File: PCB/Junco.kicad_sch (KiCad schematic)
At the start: 202 parts, among them J1 AudioJack4, J2 AudioJack4, SW1 SW_Push, SW10 SW_Push, SW11 SW_Push, SW12 SW_Push, SW13 SW_Push, SW14 SW_Push, SW15 SW_Push, SW16 SW_Push, SW17 SW_Push, SW18 SW_Push, SW19 SW_MX_Hotswap_Rotary, SW2 SW_Push, SW20 SW_Push, SW21 SW_Push, SW22 SW_Push, SW23 SW_Push, SW24 SW_Push, SW25 SW_Push, SW26 SW_Push, SW27 SW_Push, SW28 SW_Push, SW29 SW_Push, SW3 SW_Push, SW30 RotaryEncoder_Switch, SW31 SW_Push, SW32 SW_Push, SW33 SW_Push, SW34 SW_Push, SW35 SW_Push, SW36 SW_Push, SW37 SW_Push, SW38 SW_Push, SW39 SW_Push, SW4 SW_Push, SW40 SW_Push, SW41 SW_Push, SW42 SW_Push, SW43 SW_Push, SW44 SW_Push, SW45 SW_Push, SW46 SW_Push, SW47 SW_Push, SW48 SW_Push, SW49 SW_MX_Hotswap_Rotary, SW5 SW_Push, SW50 SW_Push, SW51 SW_Push, SW52 SW_Push, SW53 SW_Push, SW54 SW_Push, SW55 SW_Push, SW56 SW_Push, SW57 SW_Push, SW58 SW_Push, SW59 SW_Push, SW6 SW_Push, SW60 RotaryEncoder_Switch, SW7 SW_Push, SW8 SW_Push, SW9 SW_Push, U1 Pico, U2 SN74AHCT1G125, U3 Pico, U4 SN74AHCT1G125

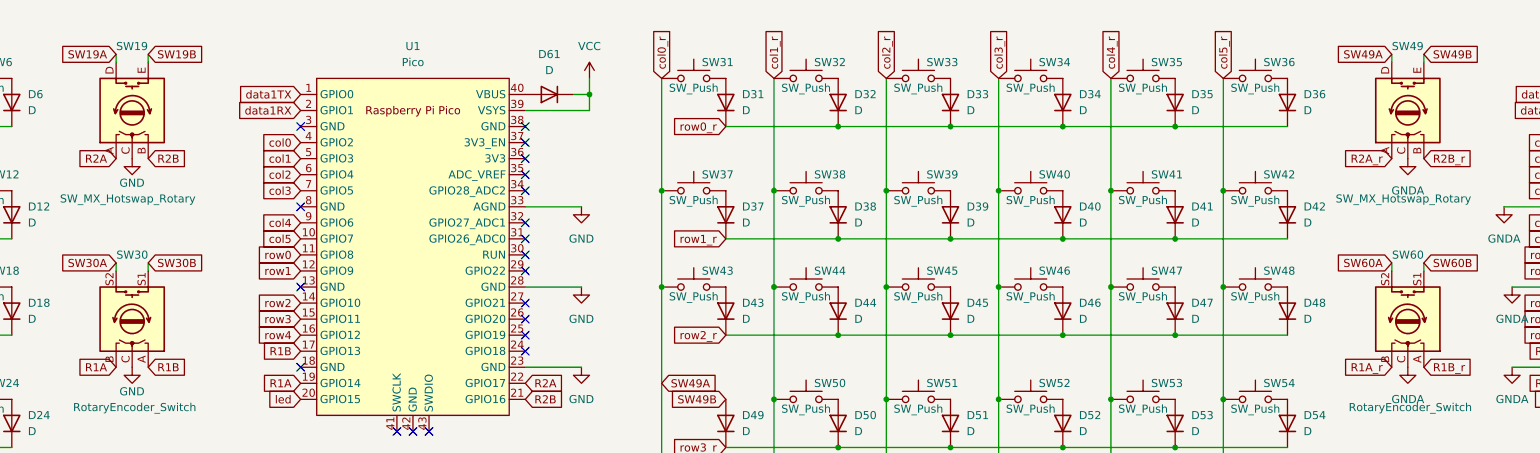
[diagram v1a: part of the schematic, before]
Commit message: Keycap rotation Swapped in smd/through-hole diode footprints
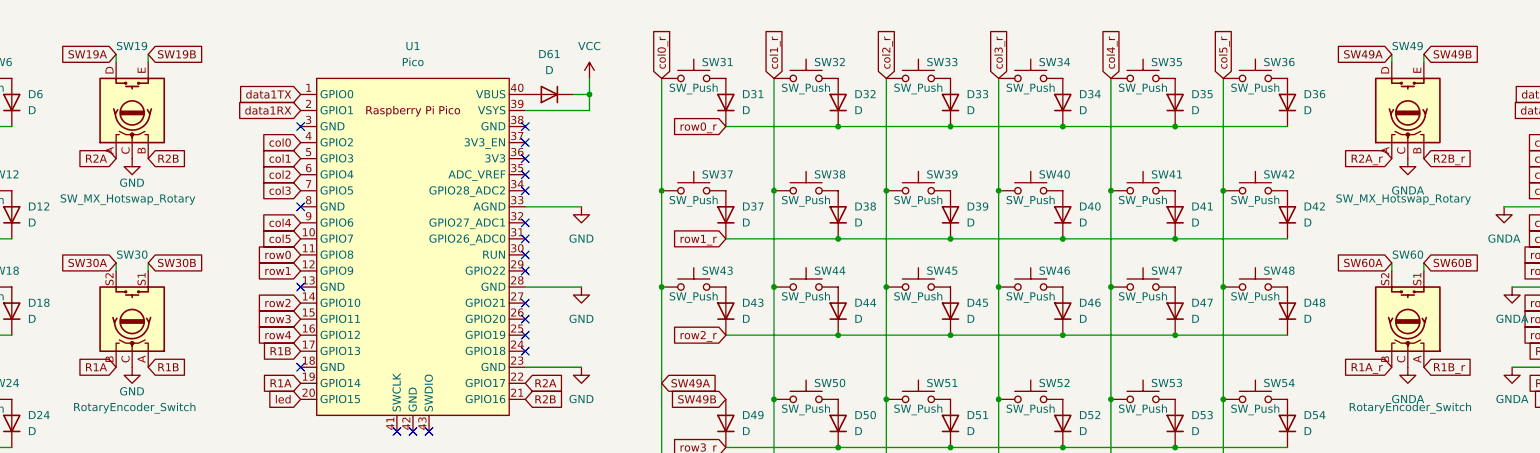
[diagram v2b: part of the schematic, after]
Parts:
- D1, D10, D11, D12, D13, D14, D15, D16, D17, D18, D19, D2, D20, D21, D22, D23, D24, D25, D26, D27, D28, D29, D3, D30, D31, D32, D33, D34, D35, D36, D37, D38, D39, D4, D40, D41, D42, D43, D44, D45, D46, D47, D48, D49, D5, D50, D51, D52, D53, D54, D55, D56, D57, D58, D59, D6, D60, D61, D62, D7, D8, D9: footprint Junco:D_SOD-123 -> Junco:D_SOD-123_DO-35_Hybrid_DoubleSided_V2

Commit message: comitt before pcb led rotation unification already updated LED orientation on schematic
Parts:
- SK68XX_Mini10, SK68XX_Mini11, SK68XX_Mini12, SK68XX_Mini13, SK68XX_Mini14, SK68XX_Mini21, SK68XX_Mini22, SK68XX_Mini23, SK68XX_Mini24, SK68XX_Mini25, SK68XX_Mini26, SK68XX_Mini35, SK68XX_Mini36, SK68XX_Mini37, SK68XX_Mini52, SK68XX_Mini53, SK68XX_Mini54, SK68XX_Mini55, SK68XX_Mini56, SK68XX_Mini57, SK68XX_Mini64, SK68XX_Mini65, SK68XX_Mini66, SK68XX_Mini67, SK68XX_Mini68, SK68XX_Mini69, SK68XX_Mini70, SK68XX_Mini71, SK68XX_Mini9: footprint Junco:SK68XXMini_Offset_Flipped -> Junco:SK68XXMini_Offset
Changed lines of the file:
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@@
       (effects (font (size 1.27 1.27)) hide)
     )
-    (property "Footprint" "Junco:SK68XXMini_Offset_Flipped" (at 387.35 165.1 0)
+    (property "Footprint" "Junco:SK68XXMini_Offset" (at 387.35 165.1 0)
       (effects (font (size 1.27 1.27)) hide)
     )
@@
       (effects (font (size 1.27 1.27)) hide)
     )
-    (property "Footprint" "Junco:SK68XXMini_Offset_Flipped" (at 52.07 175.26 0)
+    (property "Footprint" "Junco:SK68XXMini_Offset" (at 52.07 175.26 0)
       (effects (font (size 1.27 1.27)) hide)
     )
@@
       (effects (font (size 1.27 1.27)) hide)
     )
-    (property "Footprint" "Junco:SK68XXMini_Offset_Flipped" (at 359.41 205.74 0)
+    (property "Footprint" "Junco:SK68XXMini_Offset" (at 359.41 205.74 0)
       (effects (font (size 1.27 1.27)) hide)
     )
@@
       (effects (font (size 1.27 1.27)) hide)
     )
-    (property "Footprint" "Junco:SK68XXMini_Offset_Flipped" (at 31.75 236.22 0)
+    (property "Footprint" "Junco:SK68XXMini_Offset" (at 31.75 236.22 0)
       (effects (font (size 1.27 1.27)) hide)
     )
@@
       (effects (font (size 1.27 1.27)) hide)
     )
-    (property "Footprint" "Junco:SK68XXMini_Offset_Flipped" (at 59.69 154.94 0)
+    (property "Footprint" "Junco:SK68XXMini_Offset" (at 59.69 154.94 0)
       (effects (font (size 1.27 1.27)) hide)
     )
@@
       (effects (font (size 1.27 1.27)) hide)
     )
-    (property "Footprint" "Junco:SK68XXMini_Offset_Flipped" (at 339.09 226.06 0)
+    (property "Footprint" "Junco:SK68XXMini_Offset" (at 339.09 226.06 0)
       (effects (font (size 1.27 1.27)) hide)
     )
@@
       (effects (font (size 1.27 1.27)) hide)
     )
-    (property "Footprint" "Junco:SK68XXMini_Offset_Flipped" (at 31.75 154.94 0)
+    (property "Footprint" "Junco:SK68XXMini_Offset" (at 31.75 154.94 0)
       (effects (font (size 1.27 1.27)) hide)
     )
@@
       (effects (font (size 1.27 1.27)) hide)
     )
-    (property "Footprint" "Junco:SK68XXMini_Offset_Flipped" (at 24.13 215.9 0)
+    (property "Footprint" "Junco:SK68XXMini_Offset" (at 24.13 215.9 0)
       (effects (font (size 1.27 1.27)) hide)
     )
@@
       (effects (font (size 1.27 1.27)) hide)
     )
-    (property "Footprint" "Junco:SK68XXMini_Offset_Flipped" (at 367.03 226.06 0)
+    (property "Footprint" "Junco:SK68XXMini_Offset" (at 367.03 226.06 0)
       (effects (font (size 1.27 1.27)) hide)
     )
@@
       (effects (font (size 1.27 1.27)) hide)
     )
-    (property "Footprint" "Junco:SK68XXMini_Offset_Flipped" (at 115.57 195.58 0)
+    (property "Footprint" "Junco:SK68XXMini_Offset" (at 115.57 195.58 0)
       (effects (font (size 1.27 1.27)) hide)
     )
@@
       (effects (font (size 1.27 1.27)) hide)
     )
-    (property "Footprint" "Junco:SK68XXMini_Offset_Flipped" (at 87.63 195.58 0)
+    (property "Footprint" "Junco:SK68XXMini_Offset" (at 87.63 195.58 0)
       (effects (font (size 1.27 1.27)) hide)
     )
@@
       (effects (font (size 1.27 1.27)) hide)
     )
-    (property "Footprint" "Junco:SK68XXMini_Offset_Flipped" (at 115.57 154.94 0)
+    (property "Footprint" "Junco:SK68XXMini_Offset" (at 115.57 154.94 0)
       (effects (font (size 1.27 1.27)) hide)
     )
@@
       (effects (font (size 1.27 1.27)) hide)
     )
-    (property "Footprint" "Junco:SK68XXMini_Offset_Flipped" (at 359.41 165.1 0)
+    (property "Footprint" "Junco:SK68XXMini_Offset" (at 359.41 165.1 0)
       (effects (font (size 1.27 1.27)) hide)
     )
@@
       (effects (font (size 1.27 1.27)) hide)
     )
-    (property "Footprint" "Junco:SK68XXMini_Offset_Flipped" (at 59.69 195.58 0)
+    (property "Footprint" "Junco:SK68XXMini_Offset" (at 59.69 195.58 0)
       (effects (font (size 1.27 1.27)) hide)
     )
@@
       (effects (font (size 1.27 1.27)) hide)
     )
-    (property "Footprint" "Junco:SK68XXMini_Offset_Flipped" (at 303.53 165.1 0)
+    (property "Footprint" "Junco:SK68XXMini_Offset" (at 303.53 165.1 0)
       (effects (font (size 1.27 1.27)) hide)
     )
@@
       (effects (font (size 1.27 1.27)) hide)
     )
-    (property "Footprint" "Junco:SK68XXMini_Offset_Flipped" (at 311.15 226.06 0)
+    (property "Footprint" "Junco:SK68XXMini_Offset" (at 311.15 226.06 0)
       (effects (font (size 1.27 1.27)) hide)
     )
@@
       (effects (font (size 1.27 1.27)) hide)
     )
-    (property "Footprint" "Junco:SK68XXMini_Offset_Flipped" (at 303.53 205.74 0)
+    (property "Footprint" "Junco:SK68XXMini_Offset" (at 303.53 205.74 0)
       (effects (font (size 1.27 1.27)) hide)
     )
@@
       (effects (font (size 1.27 1.27)) hide)
     )
-    (property "Footprint" "Junco:SK68XXMini_Offset_Flipped" (at 394.97 185.42 0)
+    (property "Footprint" "Junco:SK68XXMini_Offset" (at 394.97 185.42 0)
       (effects (font (size 1.27 1.27)) hide)
     )
@@
       (effects (font (size 1.27 1.27)) hide)
     )
-    (property "Footprint" "Junco:SK68XXMini_Offset_Flipped" (at 387.35 205.74 0)
+    (property "Footprint" "Junco:SK68XXMini_Offset" (at 387.35 205.74 0)
       (effects (font (size 1.27 1.27)) hide)
     )
@@
       (effects (font (size 1.27 1.27)) hide)
     )
-    (property "Footprint" "Junco:SK68XXMini_Offset_Flipped" (at 394.97 226.06 0)
+    (property "Footprint" "Junco:SK68XXMini_Offset" (at 394.97 226.06 0)
       (effects (font (size 1.27 1.27)) hide)
     )
@@
       (effects (font (size 1.27 1.27)) hide)
     )
-    (property "Footprint" "Junco:SK68XXMini_Offset_Flipped" (at 331.47 205.74 0)
+    (property "Footprint" "Junco:SK68XXMini_Offset" (at 331.47 205.74 0)
       (effects (font (size 1.27 1.27)) hide)
     )
@@
       (effects (font (size 1.27 1.27)) hide)
     )
-    (property "Footprint" "Junco:SK68XXMini_Offset_Flipped" (at 331.47 165.1 0)
+    (property "Footprint" "Junco:SK68XXMini_Offset" (at 331.47 165.1 0)
       (effects (font (size 1.27 1.27)) hide)
     )
@@
       (effects (font (size 1.27 1.27)) hide)
     )
-    (property "Footprint" "Junco:SK68XXMini_Offset_Flipped" (at 24.13 175.26 0)
+    (property "Footprint" "Junco:SK68XXMini_Offset" (at 24.13 175.26 0)
       (effects (font (size 1.27 1.27)) hide)
     )
@@
       (effects (font (size 1.27 1.27)) hide)
     )
-    (property "Footprint" "Junco:SK68XXMini_Offset_Flipped" (at 31.75 195.58 0)
+    (property "Footprint" "Junco:SK68XXMini_Offset" (at 31.75 195.58 0)
       (effects (font (size 1.27 1.27)) hide)
     )
@@
       (effects (font (size 1.27 1.27)) hide)
     )
-    (property "Footprint" "Junco:SK68XXMini_Offset_Flipped" (at 59.69 236.22 0)
+    (property "Footprint" "Junco:SK68XXMini_Offset" (at 59.69 236.22 0)
       (effects (font (size 1.27 1.27)) hide)
     )
@@
       (effects (font (size 1.27 1.27)) hide)
     )
-    (property "Footprint" "Junco:SK68XXMini_Offset_Flipped" (at 87.63 154.94 0)
+    (property "Footprint" "Junco:SK68XXMini_Offset" (at 87.63 154.94 0)
       (effects (font (size 1.27 1.27)) hide)
     )
@@
       (effects (font (size 1.27 1.27)) hide)
     )
-    (property "Footprint" "Junco:SK68XXMini_Offset_Flipped" (at 367.03 185.42 0)
+    (property "Footprint" "Junco:SK68XXMini_Offset" (at 367.03 185.42 0)
       (effects (font (size 1.27 1.27)) hide)
     )
@@
       (effects (font (size 1.27 1.27)) hide)
     )
-    (property "Footprint" "Junco:SK68XXMini_Offset_Flipped" (at 24.13 256.54 0)
+    (property "Footprint" "Junco:SK68XXMini_Offset" (at 24.13 256.54 0)
       (effects (font (size 1.27 1.27)) hide)
     )
@@
       (effects (font (size 1.27 1.27)) hide)
     )
-    (property "Footprint" "Junco:SK68XXMini_Offset_Flipped" (at 52.07 215.9 0)
+    (property "Footprint" "Junco:SK68XXMini_Offset" (at 52.07 215.9 0)
       (effects (font (size 1.27 1.27)) hide)
     )

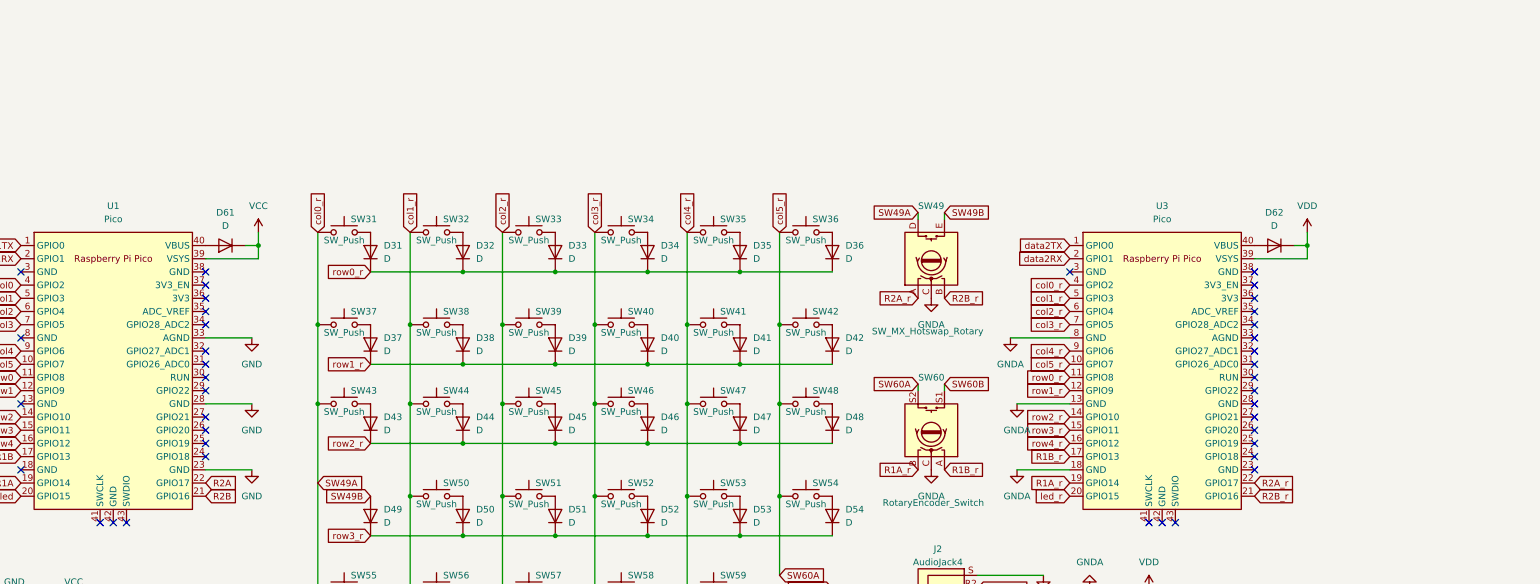
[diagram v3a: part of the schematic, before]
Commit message: Added hardware 'handedness on gp18 with default LH
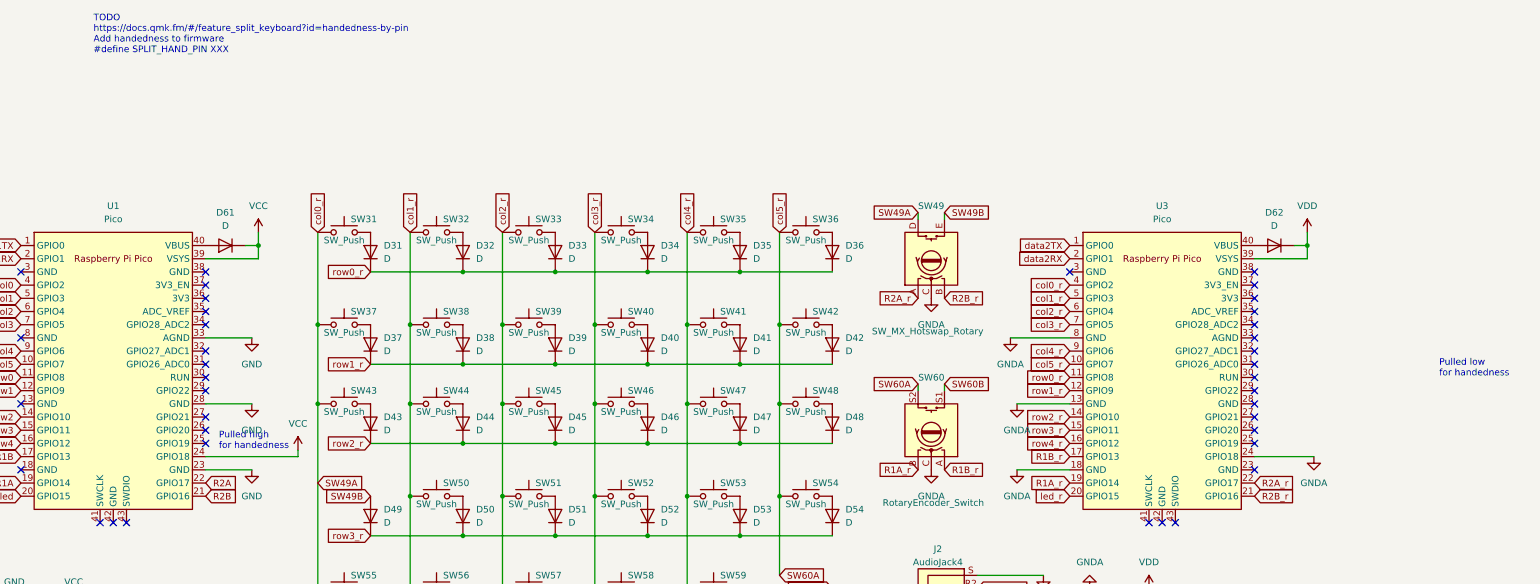
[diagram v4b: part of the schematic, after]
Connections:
- net GNDA: now also U3.24 (GPIO18)
- net VCC: now also U1.24 (GPIO18)
- no-connect marks 42 -> 40
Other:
- note added: "Pulled high for handedness"
- note added: "Pulled low for handedness"
- note added: "TODO https://docs.qmk.fm/#/feature_split_keyboard?id=handedness-by-pin Add handedness to firmware #define SPLIT_HAND_PIN XXX"
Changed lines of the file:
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@@
   )
   (no_connect (at 396.24 52.07))
-  (no_connect (at 194.31 64.77))
   (no_connect (at 194.31 62.23))
   (no_connect (at 194.31 59.69))
@@
   (no_connect (at 396.24 39.37))
   (no_connect (at 360.68 29.21))
-  (no_connect (at 396.24 64.77))
   (no_connect (at 194.31 31.75))
   (no_connect (at 176.53 77.47))
@@
     (stroke (width 0) (type default))
   )
+  (wire (pts (xy 194.31 64.77) (xy 212.09 64.77))
+    (stroke (width 0) (type default))
+  )
   (wire (pts (xy 381 215.9) (xy 403.86 215.9))
     (stroke (width 0) (type default))
@@
     (stroke (width 0) (type default))
   )
+  (wire (pts (xy 396.24 64.77) (xy 407.67 64.77))
+    (stroke (width 0) (type default))
+  )
   (wire (pts (xy 401.32 195.58) (xy 403.86 195.58))
     (stroke (width 0) (type default))
@@
     (stroke (width 0) (type default))
   )
+  (wire (pts (xy 212.09 63.5) (xy 212.09 64.77))
+    (stroke (width 0) (type default))
+  )
   (wire (pts (xy 266.7 203.2) (xy 269.24 203.2))
     (stroke (width 0) (type default))
@@
     (effects (font (size 5 5) (thickness 2) bold) (justify left bottom))
   )
+  (text "TODO\nhttps://docs.qmk.fm/#/feature_split_keyboard?id=handedness-by-pin\nAdd handedness to firmware\n#define SPLIT_HAND_PIN XXX"
+    (at 172.72 -12.7 0)
+    (effects (font (size 1.27 1.27)) (justify left bottom))
+  )
+  (text "Pulled low \nfor handedness\n" (at 431.8 49.53 0)
+    (effects (font (size 1.27 1.27)) (justify left bottom))
+  )
+  (text "Pulled high\nfor handedness\n" (at 196.85 63.5 0)
+    (effects (font (size 1.27 1.27)) (justify left bottom))
+  )
   (global_label "SW60B" (shape input) (at 314.96 90.17 180) (fields_autoplaced)
     (effects (font (size 1.27 1.27)) (justify right))
@@
     )
   )
+  (symbol (lib_id "power:VCC") (at 212.09 63.5 0) (unit 1)
+    (in_bom yes) (on_board yes) (dnp no) (fields_autoplaced)
+    (property "Reference" "#PWR03" (at 212.09 67.31 0)
+      (effects (font (size 1.27 1.27)) hide)
+    )
+    (property "Value" "VCC" (at 212.09 58.42 0)
+      (effects (font (size 1.27 1.27)))
+    )
+    (property "Footprint" "" (at 212.09 63.5 0)
+      (effects (font (size 1.27 1.27)) hide)
+    )
+    (property "Datasheet" "" (at 212.09 63.5 0)
+      (effects (font (size 1.27 1.27)) hide)
+    )
+    (pin "1")
+    (instances
+      (project "Junco"
+        (path "/c55ab6a7-e623-4136-bc89-8abb0d1fdb80"
+          (reference "#PWR03") (unit 1)
+        )
+      )
+    )
+  )
   (symbol (lib_id "Junco:SK68XXMini") (at 111.76 175.26 0) (mirror y) (unit 1)
     (in_bom yes) (on_board yes) (dnp no) (fields_autoplaced)
@@
         )
       )
+    )
+  )
+  (symbol (lib_id "power:GNDA") (at 407.67 64.77 0) (unit 1)
+    (in_bom yes) (on_board yes) (dnp no) (fields_autoplaced)
+    (property "Reference" "#PWR02" (at 407.67 71.12 0)
+      (effects (font (size 1.27 1.27)) hide)
+    )
+    (property "Value" "GNDA" (at 407.67 69.85 0)
+      (effects (font (size 1.27 1.27)))
+    )
+    (property "Footprint" "" (at 407.67 64.77 0)
+      (effects (font (size 1.27 1.27)) hide)
+    )
+    (property "Datasheet" "" (at 407.67 64.77 0)
+      (effects (font (size 1.27 1.27)) hide)
+    )
+    (pin "1")
+    (instances
+      (project "Junco"
+        (path "/c55ab6a7-e623-4136-bc89-8abb0d1fdb80"
+          (reference "#PWR02") (unit 1)
+        )
+      )
